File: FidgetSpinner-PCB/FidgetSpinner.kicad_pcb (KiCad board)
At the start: 2 copper layers, 81.9 x 90 mm, 37 parts, among them J1 DBG_CONN, J2 GP2S27, SW1 SW_POWER, SW2 button, U1 STM32L010K8T6

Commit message: updated PCB
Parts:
- turned R10 to 270 degrees
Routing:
- net Net-(J2-Pad1): track 10.8 -> 5.32 mm
- net GND: vias 76 -> 77

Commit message: bug fixes
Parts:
- removed J2: GP2S27, WYW_Package:4pin_5040
- added R15: 2M, Resistor_SMD:R_0805_2012Metric_Pad1.20x1.40mm_HandSolder, F.Cu at (92.4, 92.8)
- added U2: GP2S60, WYW_Package:GP2S60_3217, F.Cu at (96.8, 94.7)
- R10: value R_IR -> 33k
- turned R10 to 90 degrees
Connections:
- R10 pad 1: Net-(J2-Pad1) -> VCC
- R10 pad 2: VCC -> Net-(R10-Pad2)
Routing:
- net ~INT_C: track 23.5 -> 29.3 mm, vias 2 -> 4
- net VCC: track 148.6 -> 154.4 mm
- net Net-(J2-Pad1): track 5.32 -> 0.00 mm
- net GND: track 21.1 -> 26.1 mm, vias 77 -> 72
- net Net-(R10-Pad2): track 0.00 -> 4.72 mm
- net L7: track 26.8 -> 31.2 mm
- net L6: track 29.7 -> 32.5 mm
- net L2: track 42.4 -> 44.5 mm
- net L5: track 32.9 -> 33.7 mm
- net Net-(BT1-Pad1): vias 2 -> 1
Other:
- board text added: "33k"
- board text added: "8M"
- board text added: "LED FidgetSpinner v0.5.0 - (C) WYW 2021-11"
- board text removed: "260.C"
- board text removed: "PhOVS FidgetSpinner v0.4.1 - (C) WYW 2021-11-08"
- board text removed: "R-IR"

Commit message: backup
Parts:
- added R13: ?M, Resistor_SMD:R_0805_2012Metric_Pad1.20x1.40mm_HandSolder, F.Cu at (87.3, 93.9)
- added R14: ?M, Resistor_SMD:R_0805_2012Metric_Pad1.20x1.40mm_HandSolder, F.Cu at (89.7, 96.5)
- added TS881: TS881, Package_TO_SOT_SMD:SOT-353_SC-70-5, F.Cu at (89.4, 91.2)
- R15: value 2M -> ?M
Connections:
- R15 pad 1: ~INT_C -> IR_OUT
- U1 pad 22: ~INT_C -> INT_C
- U2 pad 1: ~INT_C -> IR_OUT
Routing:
- net ~INT_C: track 29.3 -> 0.00 mm, vias 4 -> 0
- net INT_C: track 0.00 -> 28.3 mm, vias 0 -> 4
- net IR_OUT: track 0.00 -> 10.4 mm
- net Net-(R13-Pad2): track 0.00 -> 7.88 mm
- net GND: track 26.1 -> 32.0 mm, vias 72 -> 73
- net VCC: track 154.4 -> 156.9 mm
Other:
- board text added: "1k1"
- board text added: "?M"
- board text added: "LED FidgetSpinner v0.7.1 - (C) WYW 2021-11"
- board text added: "TS881"
- board text removed: "8M"
- board text removed: "LED FidgetSpinner v0.5.0 - (C) WYW 2021-11"
- board text removed: "R"

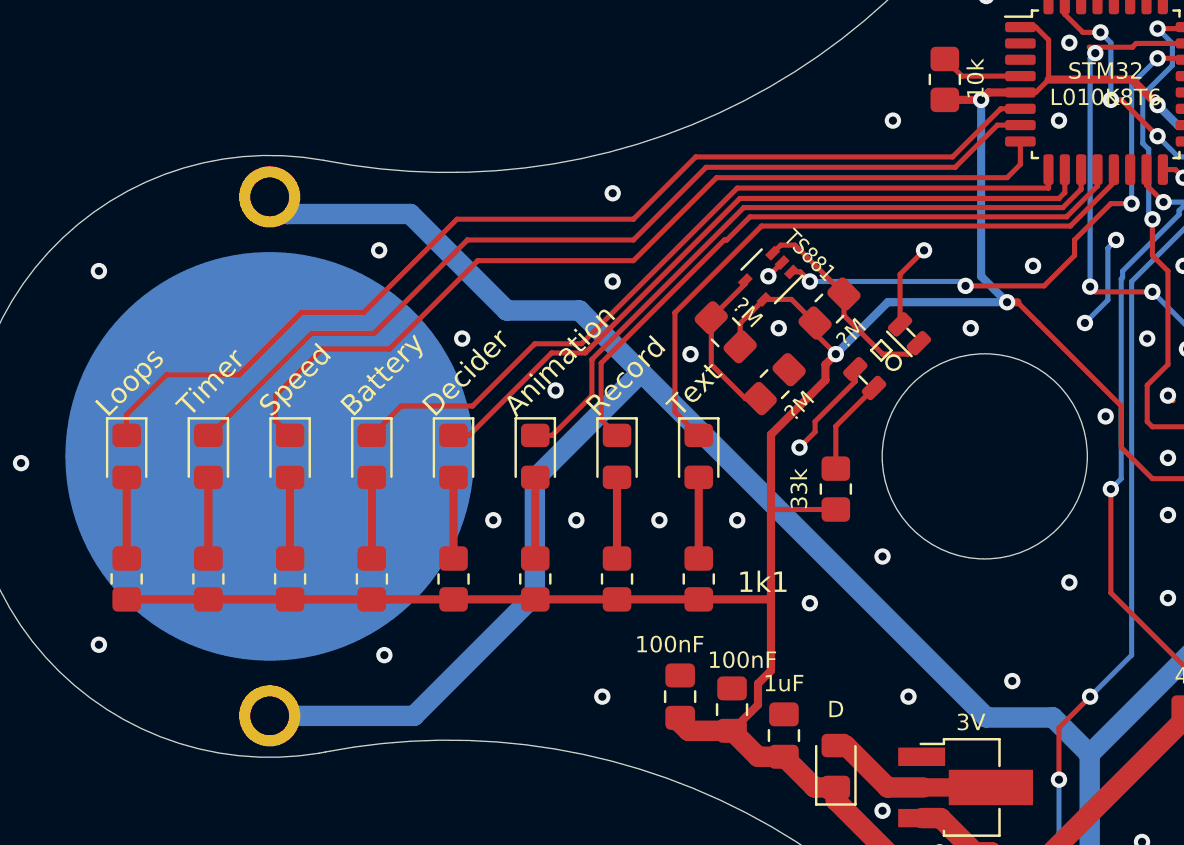
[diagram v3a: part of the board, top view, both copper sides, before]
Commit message: resistor value & firmware updates
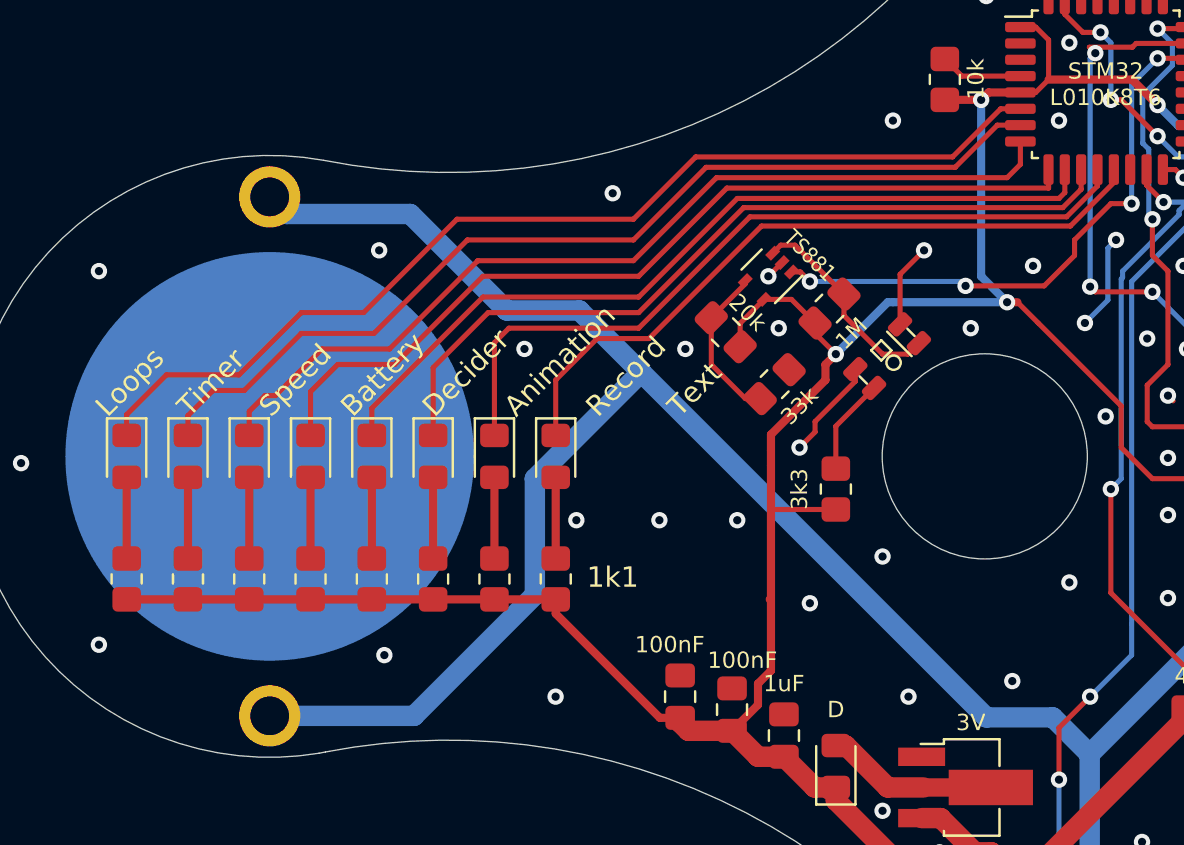
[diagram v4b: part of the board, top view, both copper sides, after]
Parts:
- moved D17 7.00 mm to (79.0, 100.0)
- moved R8 7.00 mm to (79.0, 106.0)
- moved D16 6.00 mm to (76.0, 100.0)
- moved R7 6.00 mm to (76.0, 106.0)
- moved D15 5.00 mm to (73.0, 100.0)
- moved R6 5.00 mm to (73.0, 106.0)
- moved D14 4.00 mm to (70.0, 100.0)
- moved R5 4.00 mm to (70.0, 106.0)
- moved D13 3.00 mm to (67.0, 100.0)
- moved R4 3.00 mm to (67.0, 106.0)
- moved D12 2.00 mm to (64.0, 100.0)
- moved R3 2.00 mm to (64.0, 106.0)
- moved D11 1.00 mm to (61.0, 100.0)
- moved R2 1.00 mm to (61.0, 106.0)
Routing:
- net L5: track 33.7 -> 39.6 mm
- net L6: track 32.5 -> 38.0 mm
- net L4: track 36.0 -> 40.7 mm
- net L3: track 39.2 -> 43.3 mm
- net L7: track 31.2 -> 34.7 mm
- net VCC: track 156.9 -> 155.3 mm
- net L1: track 46.0 -> 47.6 mm
- net L2: track 44.5 -> 45.0 mm
- net GND: vias 73 -> 70
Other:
- board text added: "1M"
- board text added: "20k"
- board text added: "3k3"
- board text removed: "?M"

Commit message: rearranged files
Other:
- board text added: "Pattern"
- board text removed: "Animation"
